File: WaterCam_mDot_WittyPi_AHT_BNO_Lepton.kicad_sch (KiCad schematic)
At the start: 15 parts, among them J1 GPIO, J2 Lepton Socket, J3 Conn_01x10_Socket, J4 Conn_01x10_Socket, J5 Conn_01x08_Pin, J6 Witty Pi 4 7-Pin Header, Q1 NMOS, U1 CAT24C256

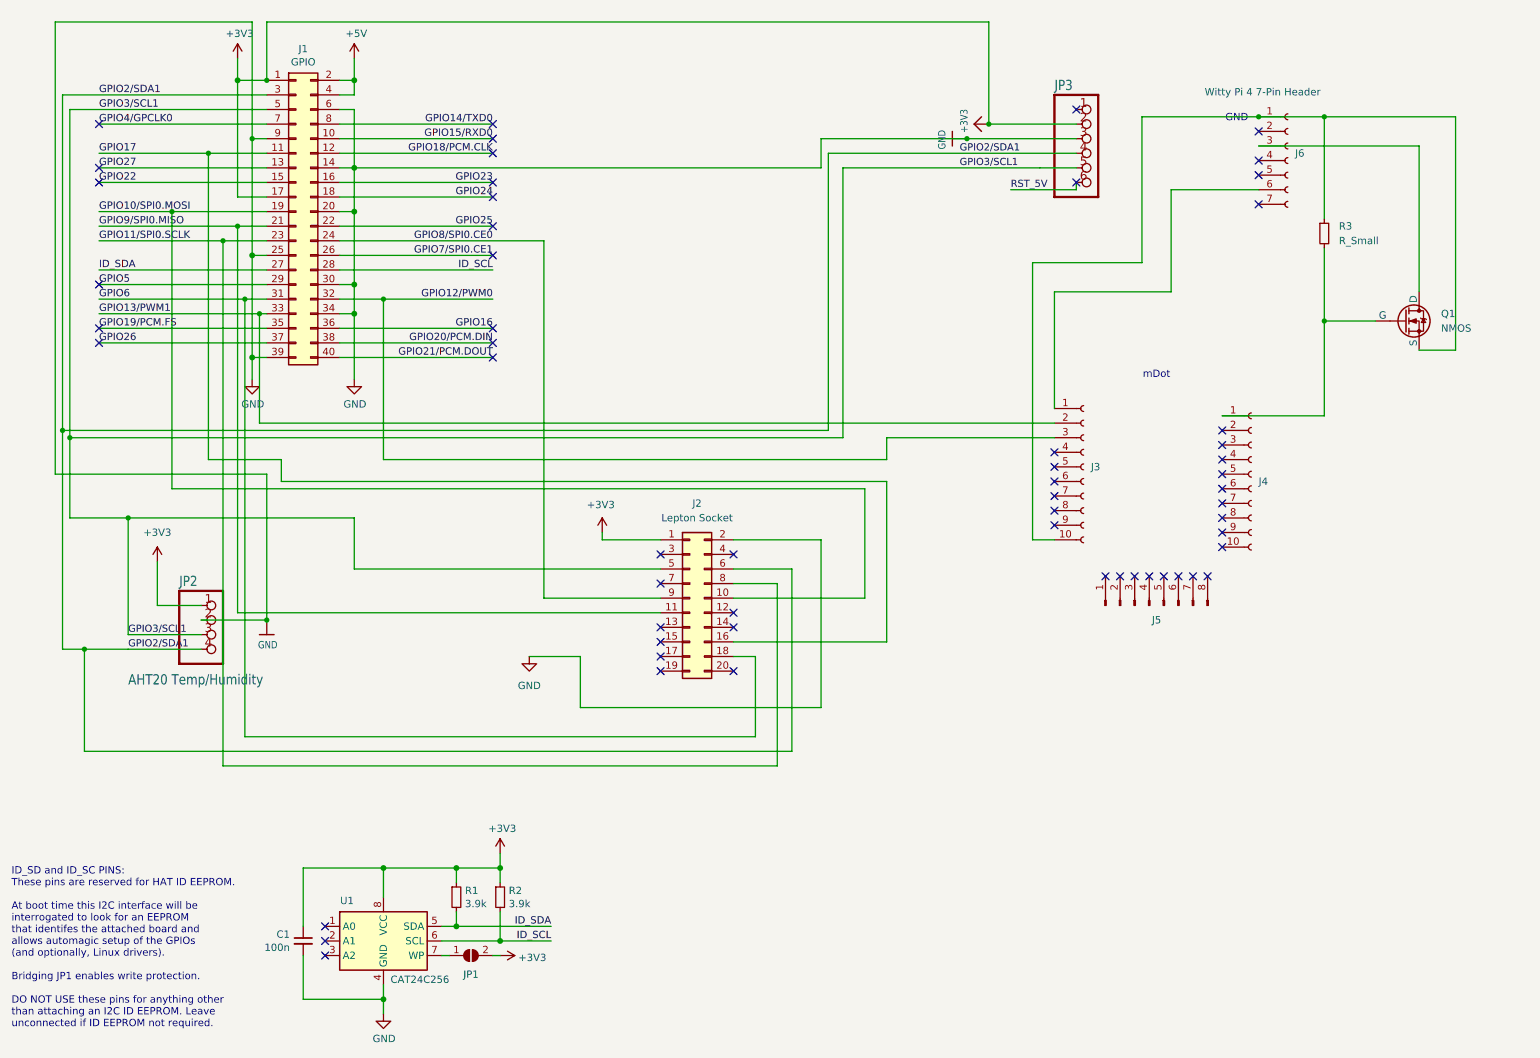
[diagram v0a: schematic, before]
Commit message: Replace power symbols with direct links to pins
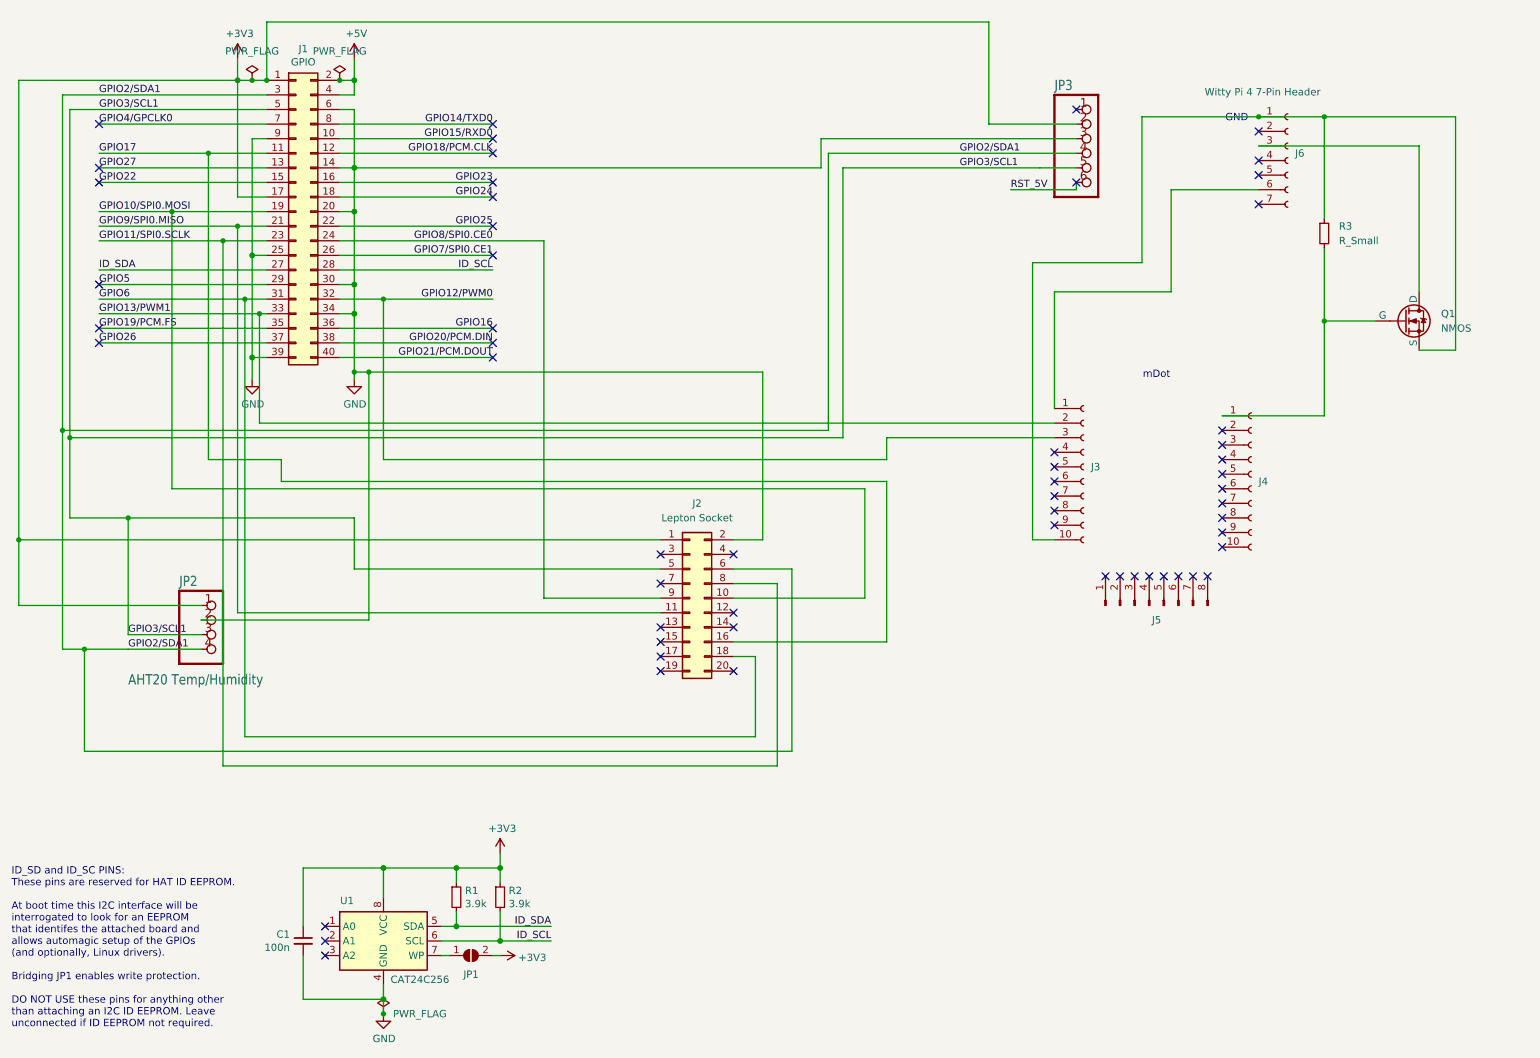
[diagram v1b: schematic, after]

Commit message: add footprints for some elements
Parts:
- J2: footprint (none) -> Connector_PinSocket_2.54mm:PinSocket_2x10_P2.54mm_Vertical
- J3, J4: footprint (none) -> Connector_PinSocket_2.00mm:PinSocket_1x10_P2.00mm_Vertical
- J5: footprint (none) -> Connector_PinHeader_2.00mm:PinHeader_1x08_P2.00mm_Vertical
- J6: footprint (none) -> Connector_PinSocket_2.54mm:PinSocket_1x07_P2.54mm_Vertical
- JP2: footprint Adafruit AHT20 Temperature & Humidity:1X04_ROUND_76 -> Connector_PinHeader_2.54mm:PinHeader_1x04_P2.54mm_Vertical
- JP3: footprint Adafruit BNO055:1X06_ROUND_76 -> Connector_PinHeader_2.54mm:PinHeader_1x04_P2.54mm_Vertical
- R3: footprint (none) -> Resistor_THT:R_Axial_DIN0207_L6.3mm_D2.5mm_P2.54mm_Vertical
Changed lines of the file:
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@@
 			)
 		)
-		(property "Footprint" ""
+		(property "Footprint" "Connector_PinSocket_2.54mm:PinSocket_1x07_P2.54mm_Vertical"
 			(at 238.76 41.91 0)
 			(effects
@@
 			)
 		)
-		(property "Footprint" "Adafruit BNO055:1X06_ROUND_76"
+		(property "Footprint" "Connector_PinHeader_2.54mm:PinHeader_1x04_P2.54mm_Vertical"
 			(at 204.47 40.64 0)
 			(effects
@@
 			)
 		)
-		(property "Footprint" "Adafruit AHT20 Temperature & Humidity:1X04_ROUND_76"
+		(property "Footprint" "Connector_PinHeader_2.54mm:PinHeader_1x04_P2.54mm_Vertical"
 			(at 52.07 124.46 0)
 			(effects
@@
 			)
 		)
-		(property "Footprint" ""
+		(property "Footprint" "Connector_PinSocket_2.00mm:PinSocket_1x10_P2.00mm_Vertical"
 			(at 232.41 96.52 0)
 			(effects
@@
 			)
 		)
-		(property "Footprint" ""
+		(property "Footprint" "Connector_PinHeader_2.00mm:PinHeader_1x08_P2.00mm_Vertical"
 			(at 214.63 119.38 0)
 			(effects
@@
 			)
 		)
-		(property "Footprint" ""
+		(property "Footprint" "Resistor_THT:R_Axial_DIN0207_L6.3mm_D2.5mm_P2.54mm_Vertical"
 			(at 245.11 54.61 0)
 			(effects
@@
 			)
 		)
-		(property "Footprint" ""
+		(property "Footprint" "Connector_PinSocket_2.00mm:PinSocket_1x10_P2.00mm_Vertical"
 			(at 203.2 95.25 0)
 			(effects
@@
 			)
 		)
-		(property "Footprint" ""
+		(property "Footprint" "Connector_PinSocket_2.54mm:PinSocket_2x10_P2.54mm_Vertical"
 			(at 134.62 118.11 0)
 			(effects

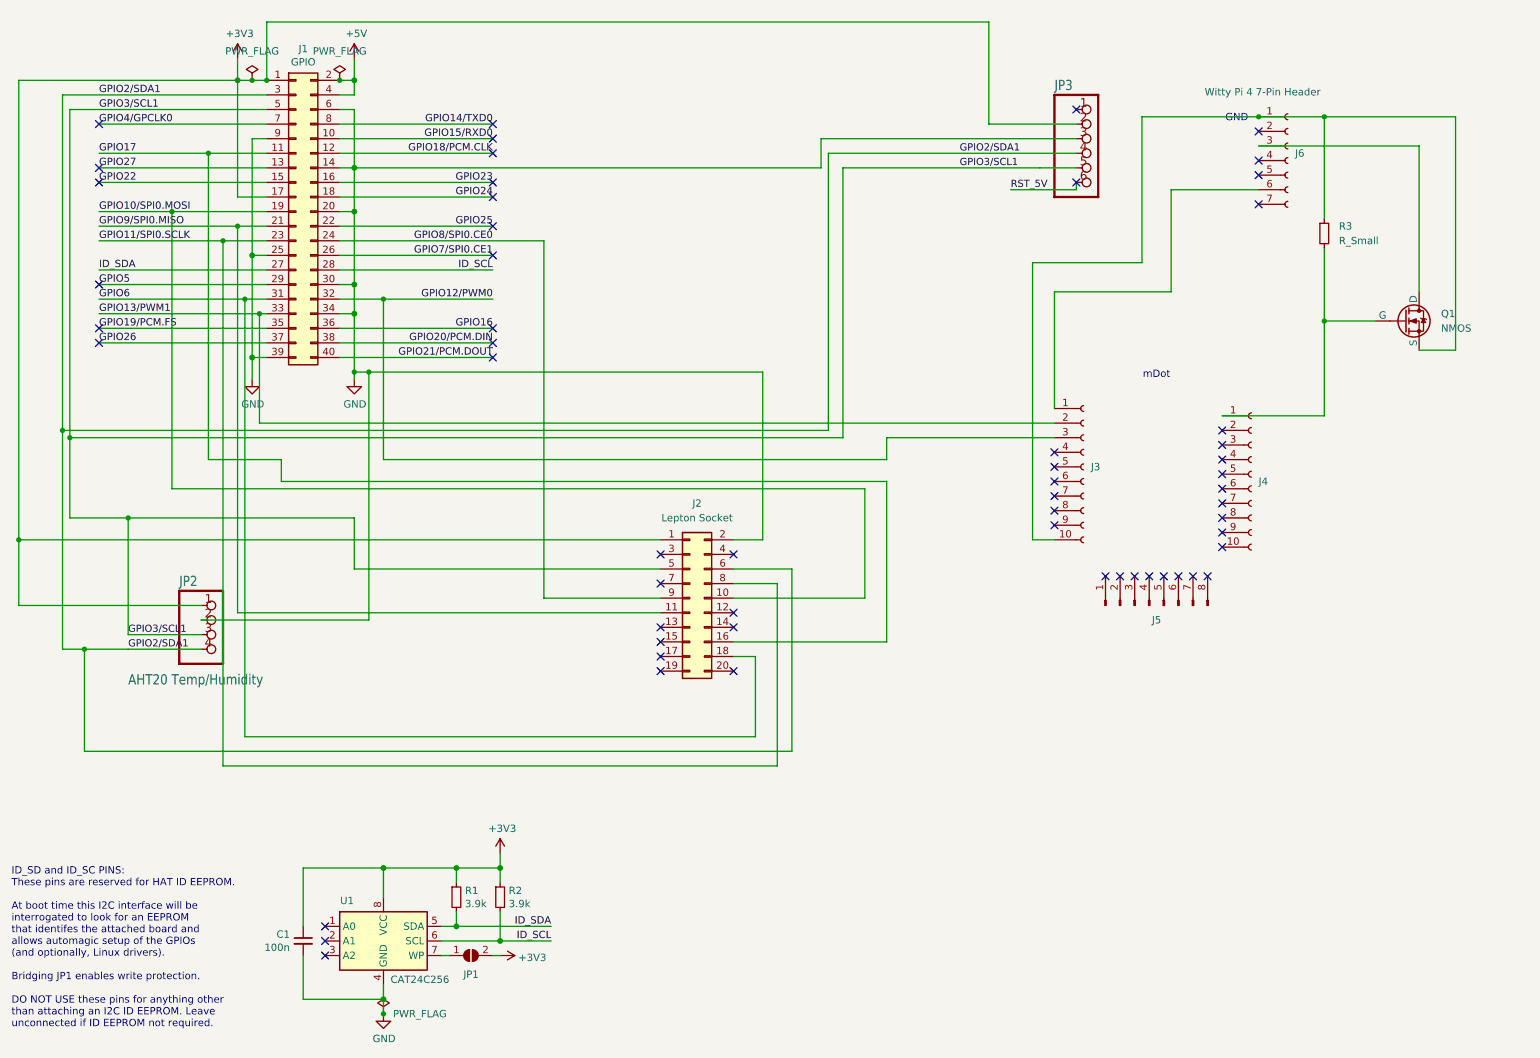
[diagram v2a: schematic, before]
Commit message: feat: complete PCB schematic
Finalize placement and routing of components. Improve labeling for clarity.
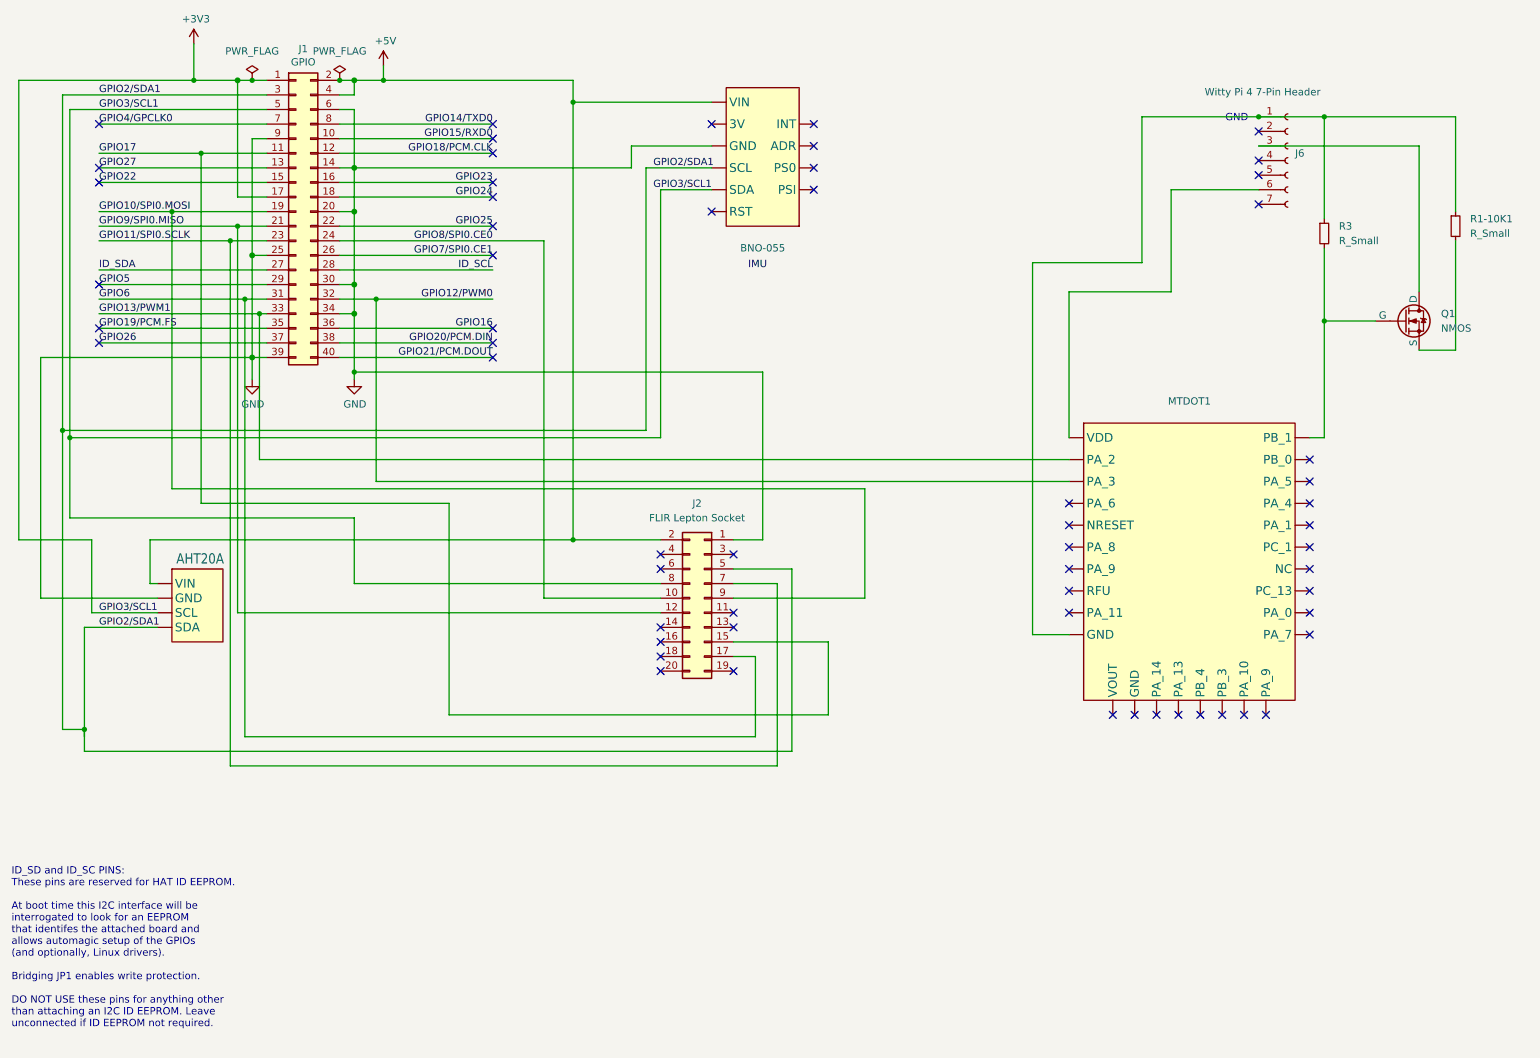
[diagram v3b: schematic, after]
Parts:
- removed C1: 100n, symbol Device:C_Small
- removed J3, J4: Conn_01x10_Socket, Connector_PinSocket_2.00mm:PinSocket_1x10_P2.00mm_Vertical, symbol Connector:Conn_01x10_Socket
- removed J5: Conn_01x08_Pin, Connector_PinHeader_2.00mm:PinHeader_1x08_P2.00mm_Vertical, symbol Connector:Conn_01x08_Pin
- removed JP1: ID_WP, symbol Jumper:SolderJumper_2_Open
- removed JP2: AHT20 Temp/Humidity, Connector_PinHeader_2.54mm:PinHeader_1x04_P2.54mm_Vertical, symbol Adafruit AHT20 Temperature & Humidity-eagle-import:HEADER-1X476MIL
- removed JP3: HEADER-1X676MIL, Connector_PinHeader_2.54mm:PinHeader_1x04_P2.54mm_Vertical, symbol Adafruit BNO055-eagle-import:microbuilder_HEADER-1X676MIL
- removed R1, R2: 3.9k, symbol Device:R_Small
- removed U1: CAT24C256, symbol Memory_EEPROM:CAT24C256
- added AHT20: ~, Adafruit AHT20 Temperature & Humidity:JST_SH4, symbol Adafruit AHT20 Temperature & Humidity-eagle-import:AHT20
- added BNO-055: ~, symbol Adafruit BNO055 STEMMA QT-eagle-import:BNO055_Simple
- added MTDOT1: ~, symbol mDOT:MTDOT-915
- added R1-10K1: R_Small, Resistor_THT:R_Axial_DIN0207_L6.3mm_D2.5mm_P2.54mm_Vertical, symbol Device:R_Small
- J2: value Lepton Socket -> FLIR Lepton Socket
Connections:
- net +3V3: now also J1.5 (Pin_5), J2.8 (Pin_8), AHT20. (SDA), BNO-055. (VIN); no longer J2.1 (Pin_1)
- net +5V: now also J2.2 (Pin_2), AHT20. (SDA), BNO-055. (VIN)
- net GND: now also J2.1 (Pin_1), AHT20. (SDA), BNO-055. (VIN); no longer J2.2 (Pin_2)
- net GPIO10/SPI0.MOSI: now also J2.9 (Pin_9); no longer J2.10 (Pin_10)
- net GPIO11/SPI0.SCLK: now also J2.7 (Pin_7); no longer J2.8 (Pin_8)
- net GPIO12/PWM0: now also MTDOT1. (PA_7)
- net GPIO13/PWM1: now also MTDOT1. (PA_7)
- net GPIO17: now also J2.15 (Pin_15); no longer J2.16 (Pin_16)
- net GPIO2/SDA1: now also J2.5 (Pin_5), AHT20. (SDA), BNO-055. (VIN); no longer J2.6 (Pin_6)
- net GPIO6: now also J2.17 (Pin_17); no longer J2.18 (Pin_18)
- net GPIO8/SPI0.CE0: now also J2.10 (Pin_10); no longer J2.9 (Pin_9)
- net GPIO9/SPI0.MISO: now also J2.12 (Pin_12); no longer J2.11 (Pin_11)
- net at J6.1 (Pin_1), R3.1: now also MTDOT1. (PA_7), R1-10K1.1; no longer Q1.3 (S)
- net at J6.6 (Pin_6): now also MTDOT1. (PA_7)
- net at Q1.2 (G), R3.2: now also MTDOT1. (PA_7)
- removed net GPIO3/SCL1: J1.5 (Pin_5), J2.5 (Pin_5)
- new net: Q1.3 (S), R1-10K1.2
- no-connect marks 58 -> 59
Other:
- note removed: "mDot"
- company: Manu Shergill -> Omar Mohammed
